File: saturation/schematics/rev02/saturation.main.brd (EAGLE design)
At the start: 89.8 x 43.2 mm, 37 parts, among them IC1 TL084P, J1 IN, J2 OUT

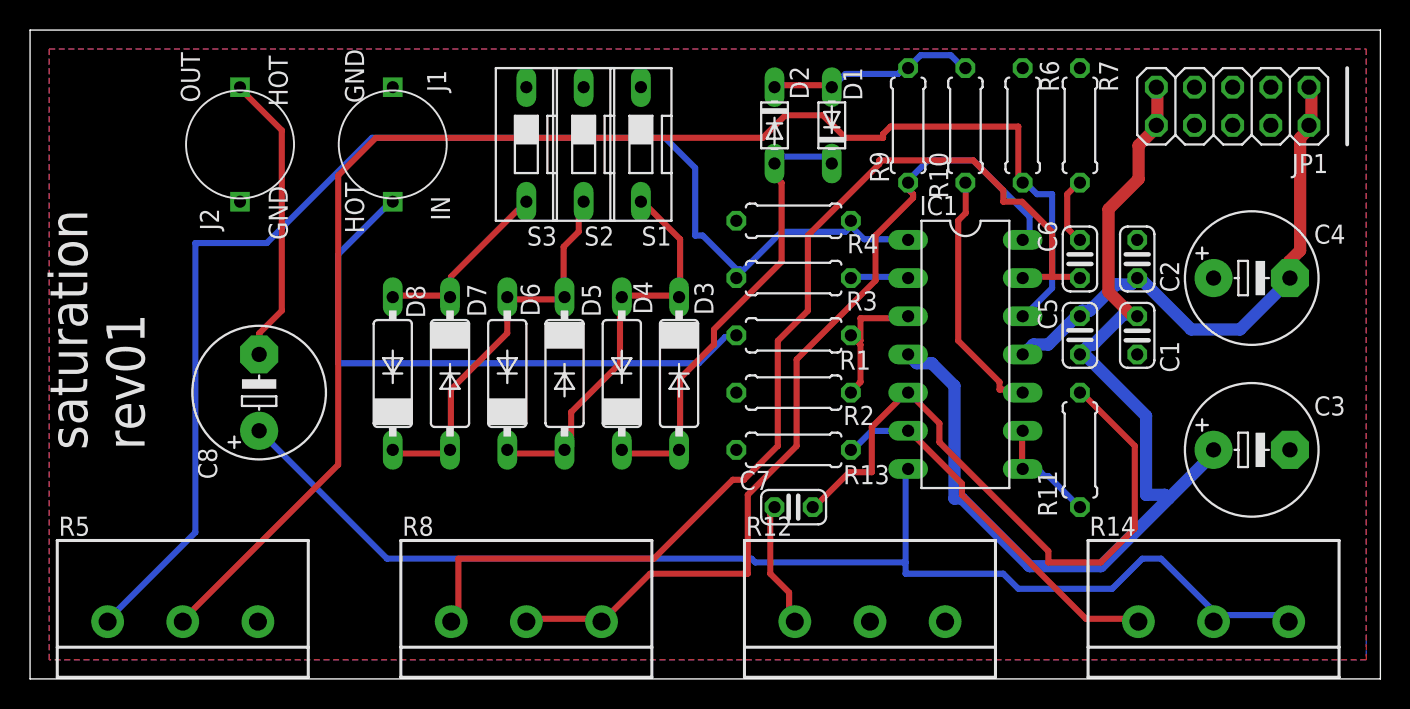
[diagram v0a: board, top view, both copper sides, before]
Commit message: Flipped sat atten pot
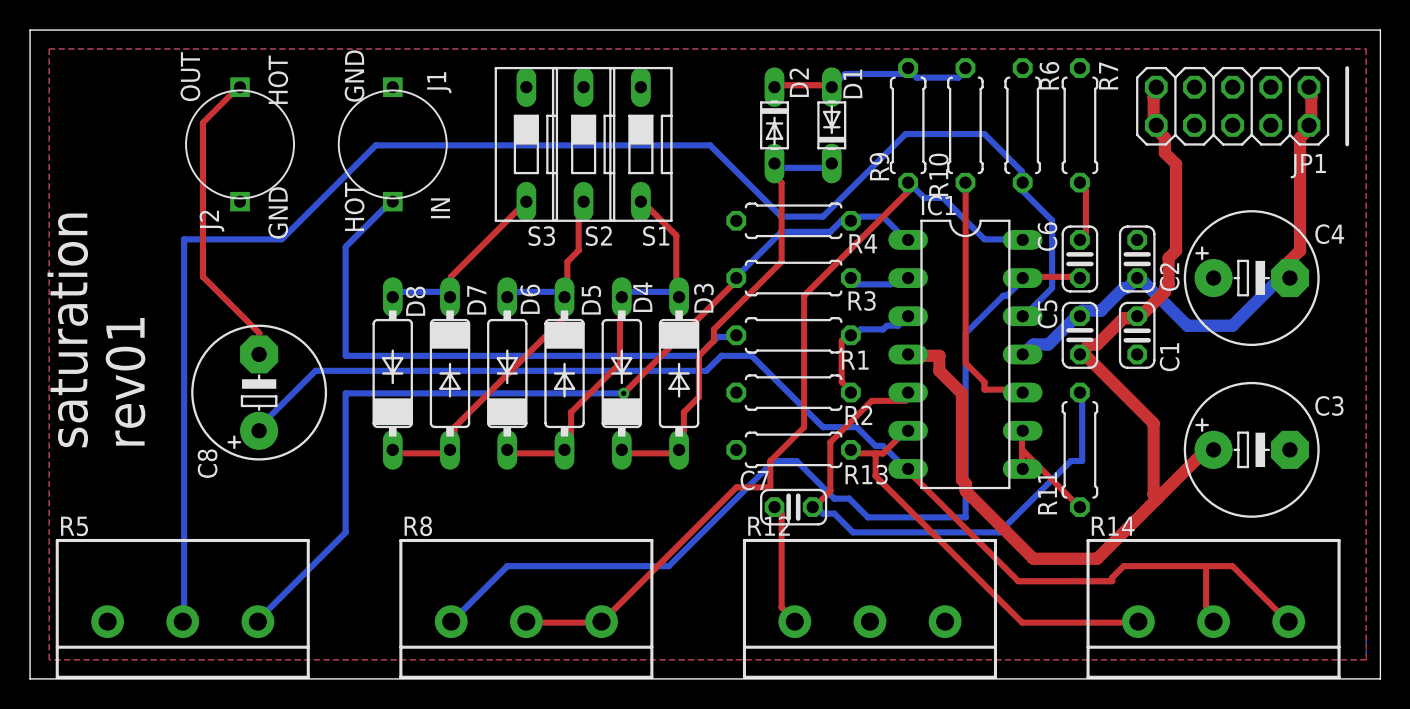
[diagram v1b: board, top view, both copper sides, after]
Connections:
- net 0V: now also R5.1; no longer R5.3
- net N$19: now also R5.3; no longer R5.1
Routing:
- net N$19: track 87.7 -> 60.7 mm, vias 0 -> 1
- net N$20: track 71.3 -> 61.7 mm
- net N$9: track 43.7 -> 36.9 mm
- net N$14: track 59.3 -> 53.3 mm
- net N$21: track 97.1 -> 100.4 mm
- net +12V: track 69.4 -> 67.1 mm
- net N$10: track 25.3 -> 27.6 mm
- net N$6: track 26.7 -> 28.5 mm
- net N$16: track 39.6 -> 38.2 mm
- net N$12: track 19.5 -> 20.4 mm
- net N$7: track 7.45 -> 8.02 mm
- net N$11: track 83.5 -> 83.0 mm
